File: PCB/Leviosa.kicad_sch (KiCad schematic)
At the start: 82 parts, among them J1 Barrel_Jack, J2 Conn_01x05_Socket, J3 2.54mm 1x03 Spare, Q1 NCE0110K, U1 SS495A, U10 TPS562201, U11 TPS61088RHLR, U2 LM321, U3 TPS1H200AQDGNRQ1, U4 LM393, U5 L78L10_SOT89, U6 MX27517, U7 AZ1117CH2-3.3, U8 INA199A3DCKR, U9 STM32G030F6Px

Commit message: DESIGN: Switch MCU to RP2040
- Added Boost, passives need adding
- Added RP2040 with clock
-deleted old 10V circuit
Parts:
- removed C5: 0.33µF, Capacitor_SMD:C_0805_2012Metric, symbol Device:C
- removed C6: 0.1uF, Capacitor_SMD:C_1206_3216Metric, symbol Device:C
- removed D8: SMF15A, Diode_SMD:D_SMF, symbol Diode:SMF15A
- removed J1: Barrel_Jack, Connector_BarrelJack:BarrelJack_Kycon_KLDX-0202-xC_Horizontal, symbol Connector:Barrel_Jack
- removed TP1: GND, TestPoint:TestPoint_Pad_D1.0mm, symbol Connector:TestPoint
- removed TP2: 12V, TestPoint:TestPoint_Pad_D1.0mm, symbol Connector:TestPoint
- removed TP4: 10V, TestPoint:TestPoint_Pad_D1.0mm, symbol Connector:TestPoint
- removed U5: L78L10_SOT89, Package_TO_SOT_SMD:SOT-89-3, symbol Regulator_Linear:L78L10_SOT89
- added C21, C23: 1uF, Capacitor_SMD:C_0603_1608Metric, symbol Device:C
- added C22, C24, C25, C26: 100nF, Capacitor_SMD:C_0603_1608Metric, symbol Device:C
- added C27, C28: 22uF, Capacitor_SMD:C_0603_1608Metric, symbol Device:C
- added J4: USB_C_Receptacle_PowerOnly_6P, symbol Connector:USB_C_Receptacle_PowerOnly_6P
- added L1: 4.7uH, symbol Device:L
- added R24, R25: 5K1, Resistor_SMD:R_0603_1608Metric, symbol Device:R_US
- added U12: RP2040, Package_DFN_QFN:QFN-56-1EP_7x7mm_P0.4mm_EP3.2x3.2mm, symbol MCU_RaspberryPi:RP2040
- added U13: MT3608, Package_TO_SOT_SMD:SOT-23-6, symbol Regulator_Switching:MT3608
- added Y1: Crystal_GND2, Crystal:Crystal_SMD_3225-4Pin_3.2x2.5mm_HandSoldering, symbol Device:Crystal_GND2
- R22: value 0 -> 140K; now fitted
- R23: value 0 -> 10K
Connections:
- net +10V: no longer C8.1, U7.1 (IN)
- net +12V: no longer R22.1
- net +12V_SF: no longer R23.1
- net +3.3V: now also C21.1, C22.1, C23.1, C24.1, U12.23 (DVDD), U12.43 (ADC_AVDD), U12.44 (VREG_VIN), U12.45 (VREG_VOUT), U12.48 (USB_VDD), U12.50 (DVDD), U12.[1,10,22,33,42,49] (IOVDD)
- net GND: now also R23.2, C21.2, C22.2, C23.2, C24.2, C25.2, C26.2, C27.2, C28.2, J4.A12 (GND), J4.B12 (GND), J4.SH (SHIELD), U12.57 (GND), U13.2 (GND), Y1.2
- net at R22.2: now also R23.1, U13.3 (FB); no longer R23.2
- new net: C25.1, U12.20 (XIN), Y1.1
- new net: C26.1, U12.21 (XOUT), Y1.3
- new net: C27.1, L1.1, U13.5 (IN)
- new net: C8.1, U7.1 (IN)
- new net: J4.B5 (CC2), R24.2
- new net: C28.1, L1.2, R22.1, U13.1 (SW)
- new net: J4.A5 (CC1), R25.2
- new net +5V: J4.A9 (VBUS), J4.B9 (VBUS), R24.1, R25.1
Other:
- note removed: "(12-10)*0.1A = 0.2W 0.2W * 55C/W = 36C"
- moved on the sheet: C17, C18, C19, C20, C4, D1, D7, FID1, FID2, FID3, H1, H2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

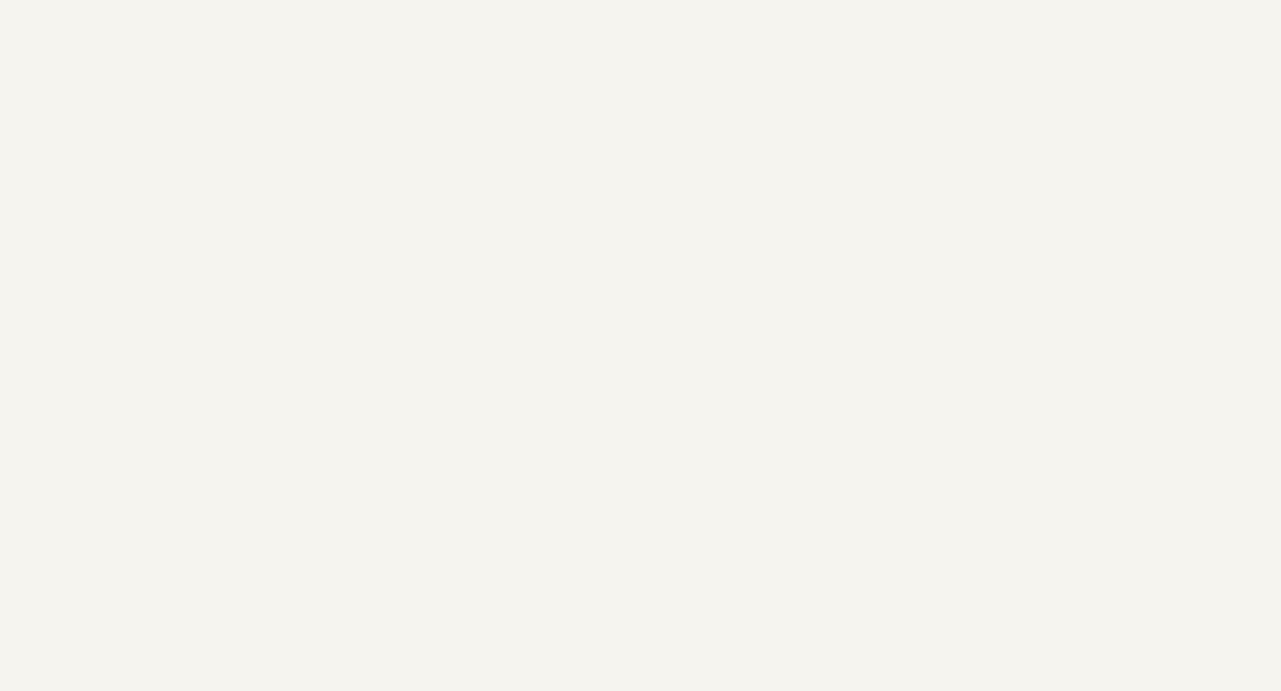
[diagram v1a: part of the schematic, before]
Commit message: DESIGN: Added RP2040
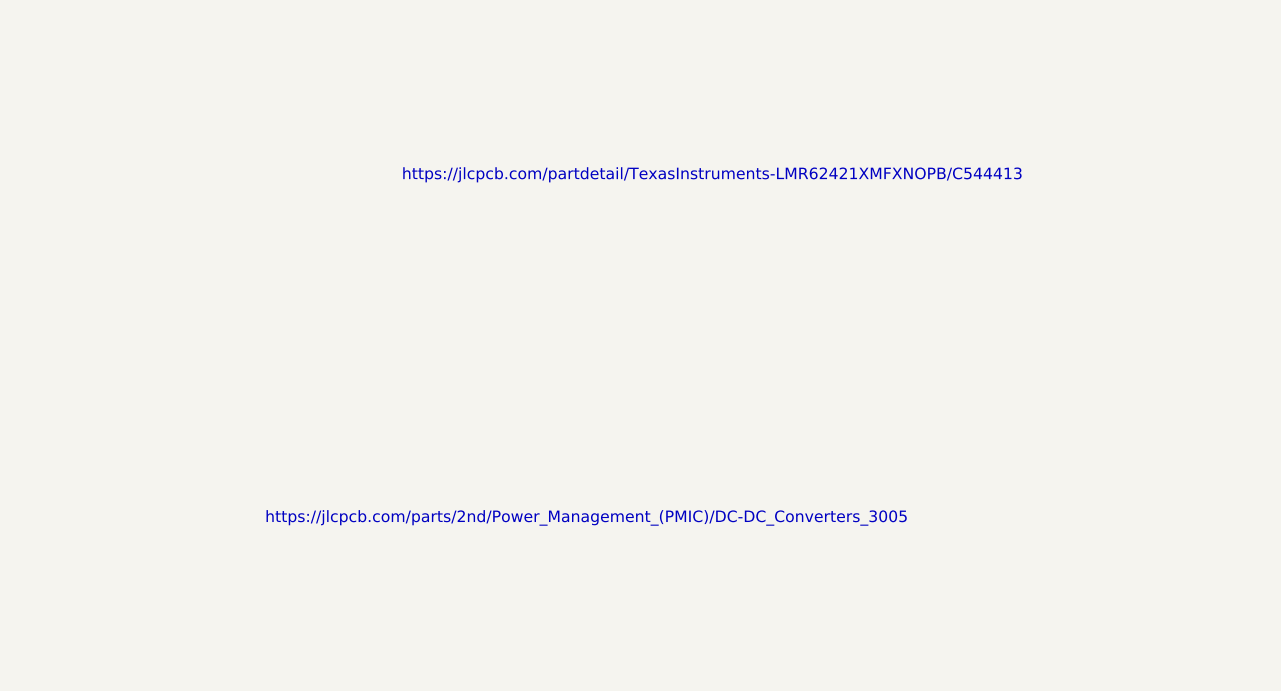
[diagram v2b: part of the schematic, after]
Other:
- note added: "https://jlcpcb.com/partdetail/TexasInstruments-LMR62421XMFXNOPB/C544413"
- note added: "https://jlcpcb.com/parts/2nd/Power_Management_(PMIC)/DC-DC_Converters_3005"
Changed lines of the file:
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@@
+		)
+	)
+	(text "https://jlcpcb.com/parts/2nd/Power_Management_(PMIC)/DC-DC_Converters_3005"
+		(exclude_from_sim no)
+		(at 187.96 -3.81 0)
+		(effects
+			(font
+				(size 1.27 1.27)
+			)
 		)
 	)
@@
 		)
 	)
+	(text "https://jlcpcb.com/partdetail/TexasInstruments-LMR62421XMFXNOPB/C544413"
+		(exclude_from_sim no)
+		(at 201.93 -41.91 0)
+		(effects
+			(font
+				(size 1.27 1.27)
+			)
+		)
+	)

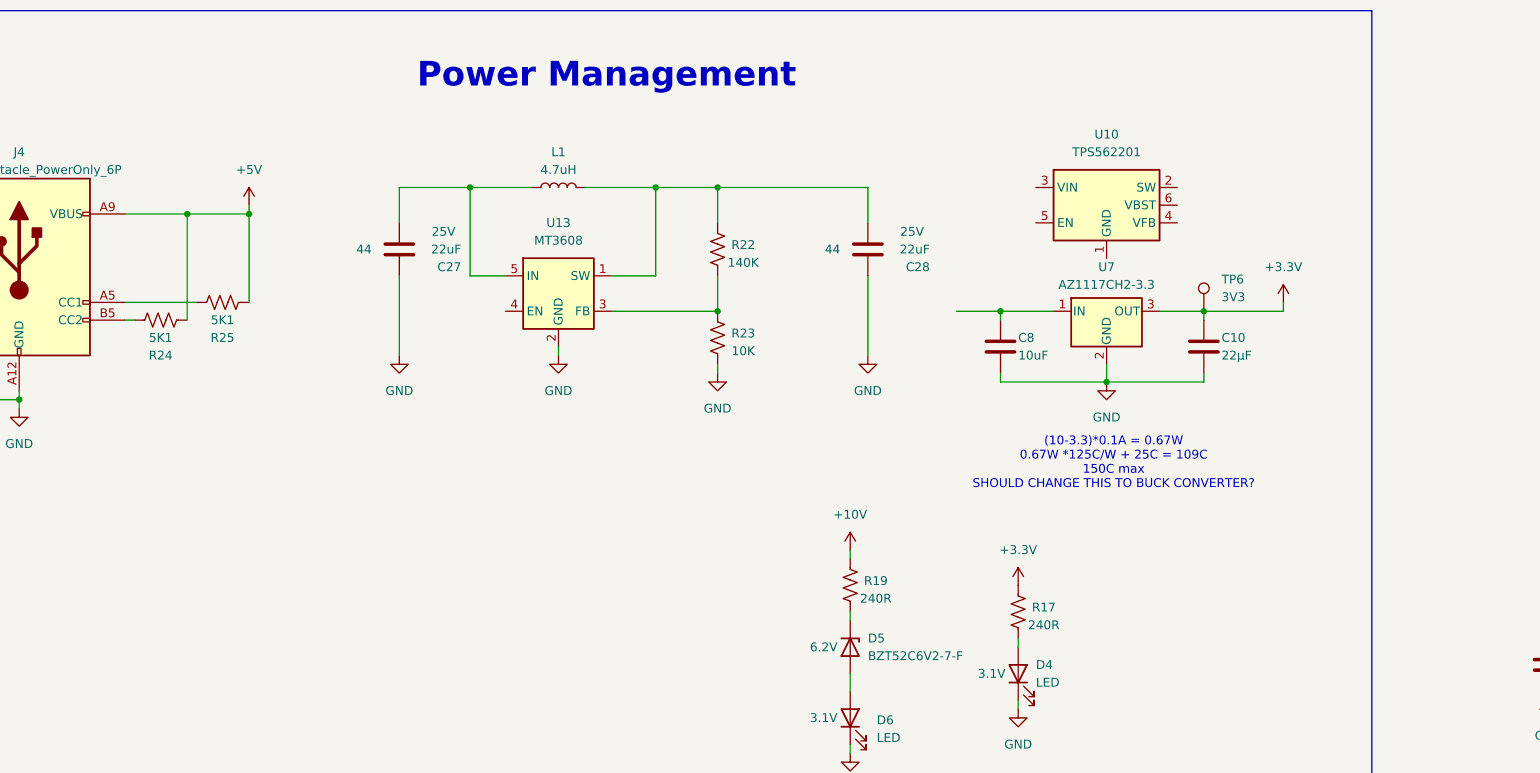
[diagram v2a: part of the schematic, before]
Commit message: DESIGN: Added 3v3 rail and links
- added 3v3 rail AP2210 (make sure to include the symbol library to the library
- Added links to current sense by TI. Seems to be similar to the last one. Just documented for now.
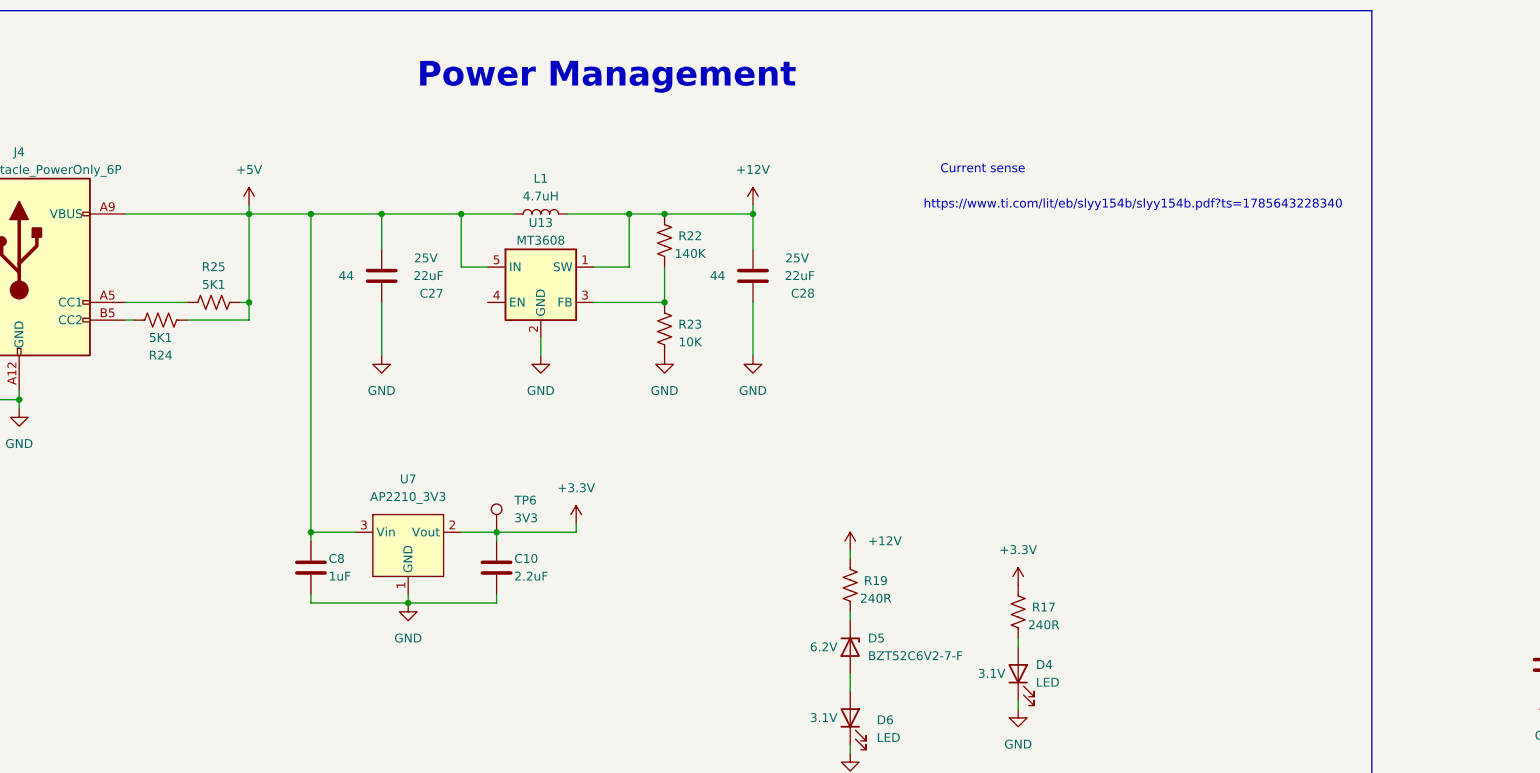
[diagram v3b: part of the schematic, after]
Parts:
- removed U10: TPS562201, Package_TO_SOT_SMD:SOT-23-6, symbol Regulator_Switching:TPS562200
- removed U7: AZ1117CH2-3.3, Package_TO_SOT_SMD:SOT-223-3_TabPin2, symbol Regulator_Linear:AZ1117CH2-3.3
- added U7: AP2210_3V3, symbol Leviosa:AP2210_3V3
- C10: value 22µF -> 2.2uF
- C8: value 10uF -> 1uF
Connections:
- net +10V: no longer R19.1
- net +12V: now also C28.1, L1.2, R19.1, R22.1, U13.1 (SW)
- net +3.3V: now also U7.2 (Vout)
- net +5V: now also C27.1, C8.1, L1.1, R25.2, U13.5 (IN), U7.3 (Vin); no longer R25.1
- net GND: now also U7.1 (GND)
- net at J4.A5 (CC1): now also R25.1; no longer R25.2
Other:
- note added: "Current sense"
- note added: "https://www.ti.com/lit/eb/slyy154b/slyy154b.pdf?ts=1785643228340"
- note removed: "(10-3.3)*0.1A = 0.67W 0.67W *125C/W + 25C = 109C 150C max SHOULD CHANGE THIS TO BUCK CONVERTER?"
- moved on the sheet: C10, C27, C28, C8, L1, R22, R23, R25, TP6, U13

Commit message: IMP: simplify. Update boost, change logic circuit to 5V.
Changed boost to one that is more thermally resilient.
Added back current limiter.
Changed analog logic circuit to 5V.
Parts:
- removed D1: LED, LED_SMD:LED_0805_2012Metric, symbol Device:LED
- removed R8: 3K9, Resistor_SMD:R_0603_1608Metric, symbol Device:R_US
- removed TP3: 12_Safe, TestPoint:TestPoint_Pad_D1.0mm, symbol Connector:TestPoint
- added C30, C31: 47uF, Capacitor_SMD:C_1210_3225Metric_Pad1.33x2.70mm_HandSolder, symbol Device:C
- added C5: 560pF, Capacitor_SMD:C_0805_2012Metric, symbol Device:C
- added D8: SS34, Diode_SMD:D_SMA_Handsoldering, symbol Diode:SS34
- added D9: LED, LED_SMD:LED_0805_2012Metric, symbol Device:LED
- added L2: 22uH, symbol Device:L
- added R26: 86.6k, Resistor_SMD:R_0201_0603Metric_Pad0.64x0.40mm_HandSolder, symbol Device:R_US
- added R27, R28: 10k, Resistor_SMD:R_0201_0603Metric_Pad0.64x0.40mm_HandSolder, symbol Device:R_US
- added R29: 3K9, Resistor_SMD:R_0603_1608Metric, symbol Device:R_US
- added TP4: 12_Safe, TestPoint:TestPoint_Pad_D1.0mm, symbol Connector:TestPoint
- added U5: LMR62421XMF, Package_TO_SOT_SMD:SOT-23-5, symbol Regulator_Switching:LMR62421XMF
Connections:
- net +10V is gone; now on net +5V: C1.1, C2.1, C7.1, R1.2, R4.2, R9.2, U1.1 (VCC), U2.5 (V+), U4.8 (V+), U6.1 (VCC)
- net +12V: now also C31.2, C5.2, D8.1 (K), R26.2
- net +12V_SF: now also C14.1, COIL1.1, D3.1 (K), D9.2 (A), TP4.1
- net +5V: now also C30.2, L2.1, R28.1, U5.5 (VIN); no longer C27.1, C8.1, L1.1, U13.5 (IN), U7.3 (Vin)
- net GND: now also C30.1, C31.1, R27.2, R29.2, U5.2 (GND)
- new net: C5.1, R26.1, R27.1, U5.3 (FB)
- new net: C27.1, L1.1, U13.5 (IN)
- new net: C8.1, U7.3 (Vin)
- new net: R28.2, U5.4 (EN)
- new net: D8.2 (A), L2.2, U5.1 (SW)
- new net: D9.1 (K), R29.1
- new net: R13.2, R15.1
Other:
- moved on the sheet: C27, C28, C4, D2, D4, D5, D6, J4, L1, R11, R17, R19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

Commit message: IMP: various updates and changes. WIP
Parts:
- added R30: X, Resistor_SMD:R_0805_2012Metric_Pad1.20x1.40mm_HandSolder, symbol Device:R_US
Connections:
- net COIL_OUT: now also R30.1; no longer D3.2 (A)
- new net: D3.2 (A), R30.2
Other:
- note added: "why remove the resistor in seires with the diode?"
- moved on the sheet: D3
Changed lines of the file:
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@@
 				(bold yes)
 			)
-			(href "https://www.ti.com/document-viewer/lit/html/SSZTBC7")
 		)
 	)
@@
 		)
 	)
+	(text "why remove the resistor in seires with the diode?"
+		(exclude_from_sim no)
+		(at 237.236 187.706 0)
+		(effects
+			(font
+				(size 1.27 1.27)
+			)
+		)
+	)
 	(text "20nF prev used\n"
 		(exclude_from_sim no)
@@
 	)
 	(junction
-		(at 222.25 209.55)
+		(at 69.85 229.87)
 		(diameter 0)
 		(color 0 0 0 0)
 	)
 	(junction
-		(at 69.85 229.87)
+		(at 222.25 209.55)
 		(diameter 0)
 		(color 0 0 0 0)
@@
 	)
 	(junction
-		(at 222.25 191.77)
-		(diameter 0)
-		(color 0 0 0 0)
-	)
-	(junction
 		(at 618.49 195.58)
 		(diameter 0)
@@
 	)
 	(junction
+		(at 222.25 191.77)
+		(diameter 0)
+		(color 0 0 0 0)
+	)
+	(junction
 		(at 30.48 213.36)
 		(diameter 0)
@@
 	(wire
 		(pts
-			(xy 222.25 203.2) (xy 222.25 209.55)
+			(xy 222.25 200.66) (xy 222.25 201.93)
 		)
 		(stroke
@@
 	(wire
 		(pts
-			(xy 222.25 191.77) (xy 222.25 195.58)
+			(xy 222.25 191.77) (xy 222.25 193.04)
 		)
 		(stroke
@@
 	)
 	(symbol
+		(lib_id "Device:R_US")
+		(at 222.25 205.74 180)
+		(unit 1)
+		(body_style 1)
+		(exclude_from_sim no)
+		(in_bom yes)
+		(on_board yes)
+		(in_pos_files yes)
+		(dnp no)
+		(property "Reference" "R30"
+			(at 227.33 204.47 0)
+			(show_name no)
+			(do_not_autoplace no)
+			(effects
+				(font
+					(size 1.27 1.27)
+				)
+			)
+		)
+		(property "Value" "X"
+			(at 227.33 207.01 0)
+			(show_name no)
+			(do_not_autoplace no)
+			(effects
+				(font
+					(size 1.27 1.27)
+				)
+			)
+		)
+		(property "Footprint" "Resistor_SMD:R_0805_2012Metric_Pad1.20x1.40mm_HandSolder"
+			(at 221.234 205.486 90)
+			(hide yes)
+			(show_name no)
+			(do_not_autoplace no)
+			(effects
+				(font
+					(size 1.27 1.27)
+				)
+			)
+		)
+		(property "Datasheet" ""
+			(at 222.25 205.74 0)
+			(hide yes)
+			(show_name no)
+			(do_not_autoplace no)
+			(effects
+				(font
+					(size 1.27 1.27)
+				)
+			)
+		)
+		(property "Description" ""
+			(at 222.25 205.74 0)
+			(show_name no)
+			(do_not_autoplace no)
+			(effects
+				(font
+					(size 1.27 1.27)
+				)
+			)
+		)
+		(property "Link" ""
+			(at 222.25 205.74 90)
+			(hide yes)
+			(show_name no)
+			(do_not_autoplace no)
+			(effects
+				(font
+					(size 1.27 1.27)
+				)
+			)
+		)
+		(pin "1"
+		)
+		(pin "2"
+		)
+		(instances
+			(project "Leviosa"
+				(path "/fe766911-203b-467c-b704-d4bd488f6c98"
+					(reference "R30")
+					(unit 1)
+				)
+			)
+		)
+	)
+	(symbol
 		(lib_id "TPS61088:TPS61088RHLR")
 		(at -80.01 50.8 0)
@@
 	(symbol
 		(lib_id "Diode:SS34")
-		(at 222.25 199.39 270)
+		(at 222.25 196.85 270)
 		(unit 1)
 		(body_style 1)
@@
 		(dnp no)
 		(property "Reference" "D3"
-			(at 214.63 198.12 90)
+			(at 214.63 195.58 90)
 			(show_name no)
 			(do_not_autoplace no)
@@
 		)
 		(property "Value" "SS34"
-			(at 214.63 200.66 90)
+			(at 214.63 198.12 90)
 			(show_name no)
 			(do_not_autoplace no)
@@
 		)
 		(property "Footprint" "Diode_SMD:D_SMA_Handsoldering"
-			(at 217.805 199.39 0)
+			(at 217.805 196.85 0)
 			(hide yes)
 			(show_name no)
@@
 		)
 		(property "Datasheet" "file://${KIPRJMOD}/datasheets/ss32.pdf"
-			(at 222.25 199.39 0)
+			(at 222.25 196.85 0)
 			(hide yes)
 			(show_name no)
@@
 		)
 		(property "Description" "40V 3A Schottky Diode, SMA"
-			(at 222.25 199.39 0)
+			(at 222.25 196.85 0)
 			(hide yes)
 			(show_name no)
@@
 		)
 		(property "Link" "https://jlcpcb.com/partdetail/MDD_Microdiode_Semiconductor-SS34/C8678"
-			(at 222.25 199.39 90)
+			(at 222.25 196.85 90)
 			(hide yes)
 			(show_name no)
@@
 		)
 		(property "Link2" "https://www.lcsc.com/product-detail/C8678.html?s_z=n_SS34&spm=wm.ssy.bg.2.xh&lcsc_vid=FgBdVFcAFQddBlFSEgVbXlBXRVlWBlZWRABaUgJXFgAxVlNRQ1RWV1BUQVdZVDsOAxUeFF5JWBYZEEoKFBINSQcJGk4%3D"
-			(at 222.25 199.39 90)
+			(at 222.25 196.85 90)
 			(hide yes)
 			(show_name no)

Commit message: cleanup and erc fixes. ready for pcb design
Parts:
- removed C10: 2.2uF, Capacitor_SMD:C_0805_2012Metric, symbol Device:C
- removed C11, C12: 0.1uF, Capacitor_SMD:C_0805_2012Metric, symbol Device:C
- removed C15: 0.1µF, Capacitor_SMD:C_0603_1608Metric, symbol Device:C
- removed C16: 0.1uF, Capacitor_SMD:C_1206_3216Metric, symbol Device:C
- removed C17: 4.7uF, Capacitor_SMD:C_0805_2012Metric, symbol Device:C
- removed C18, C22, C24, C25, C26: 100nF, Capacitor_SMD:C_0603_1608Metric, symbol Device:C
- removed C19, C20: 22µF, Capacitor_SMD:C_0805_2012Metric, symbol Device:C
- removed C21, C23: 1uF, Capacitor_SMD:C_0603_1608Metric, symbol Device:C
- removed C27, C28: 22uF, Capacitor_SMD:C_0603_1608Metric, symbol Device:C
- removed C8: 1uF, Capacitor_SMD:C_0805_2012Metric, symbol Device:C
- removed D4, D7: LED, LED_SMD:LED_0603_1608Metric, symbol Device:LED
- removed J2: Conn_01x05_Socket, Connector_PinHeader_2.54mm:PinHeader_1x05_P2.54mm_Vertical, symbol Connector:Conn_01x05_Socket
- removed J3: 2.54mm 1x03 Spare, Connector_PinHeader_2.54mm:PinHeader_1x03_P2.54mm_Vertical, symbol Connector_Generic:Conn_01x03
- removed L1: 4.7uH, symbol Device:L
- removed R13: 50mΩ, Resistor_SMD:R_2010_5025Metric, symbol Device:R_US
- removed R14, R15: 8.2Ω, Resistor_SMD:R_0805_2012Metric, symbol Device:R_US
- removed R17, R21: 240R, Resistor_SMD:R_0603_1608Metric, symbol Device:R_US
- removed R20: 3K9, Resistor_SMD:R_0603_1608Metric, symbol Device:R_US
- removed R22: 140K, Resistor_SMD:R_0603_1608Metric, symbol Device:R_US
- removed R23: 10K, Resistor_SMD:R_0603_1608Metric, symbol Device:R_US
- removed SRV1, SRV2: 2.54mm 1x03 Servo 1, Connector_PinHeader_2.54mm:PinHeader_1x03_P2.54mm_Vertical, symbol Connector_Generic:Conn_01x03
- removed TP6: 3V3, TestPoint:TestPoint_Pad_D1.0mm, symbol Connector:TestPoint
- removed TP7: COIL_OUT, TestPoint:TestPoint_Pad_D1.0mm, symbol Connector:TestPoint
- removed U11: TPS61088RHLR, TPS61088:RHL0020A, symbol TPS61088:TPS61088RHLR
- removed U12: RP2040, Package_DFN_QFN:QFN-56-1EP_7x7mm_P0.4mm_EP3.2x3.2mm, symbol MCU_RaspberryPi:RP2040
- removed U13: MT3608, Package_TO_SOT_SMD:SOT-23-6, symbol Regulator_Switching:MT3608
- removed U7: AP2210_3V3, symbol Leviosa:AP2210_3V3
- removed U8: INA199A3DCKR, Package_TO_SOT_SMD:SOT-363_SC-70-6_Handsoldering, symbol Amplifier_Current:INA199xxDCK
- removed U9: STM32G030F6Px, Package_SO:TSSOP-20_4.4x6.5mm_P0.65mm, symbol MCU_ST_STM32G0:STM32G030F6Px
- removed Y1: Crystal_GND2, Crystal:Crystal_SMD_3225-4Pin_3.2x2.5mm_HandSoldering, symbol Device:Crystal_GND2
- added TP2: COIL_OUT, TestPoint:TestPoint_Pad_D1.0mm, symbol Connector:TestPoint
- L1: renamed from L2; footprint (none) -> Inductor_SMD:L_APV_APH0615
- renumbered C13 to C10, C14 to C11, C30 to C3, C3 to C4, C31 to C6, C9 to C8, C4 to C9, D8 to D1, D5 to D4, D6 to D5, D9 to D6, J4 to J1, R27 to R10, R26 to R11, R10 to R12, R3 to R13, R12 to R14, R11 to R15, R7 to R16, R30 to R17, R16 to R18, R18 to R19, R19 to R20, R29 to R21, R24 to R3, R25 to R4, R6 to R5, R4 to R6, R5 to R7, R28 to R8, TP5 to TP1, TP4 to TP3, U4 to U3, U5 to U4, U6 to U5, U3 to U6
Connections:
- net GND: now also TP2.1
- net FAULT: no longer names the net of U6.3 (~{FAULT})
- no-connect marks 8 -> 2
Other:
- note added: "I think we should make this around 500K"
- note removed: "MCU"
- note removed: "Sense Output RC filter: R9 == R10 < 10Ω Fc = 1/ (2pi * R * C) let R = 3.9kΩ and C = 0.1μF Fc = 408Hz"
- moved on the sheet: C9
